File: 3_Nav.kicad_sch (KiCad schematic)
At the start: 38 parts, among them J401 GNSS, Q401 Q_NMOS, SW401 SW_Push, SW402 SW_Push, U403 STM32F446VETx, U404 W25Q128JVE, Y401 YXC YSX321SL

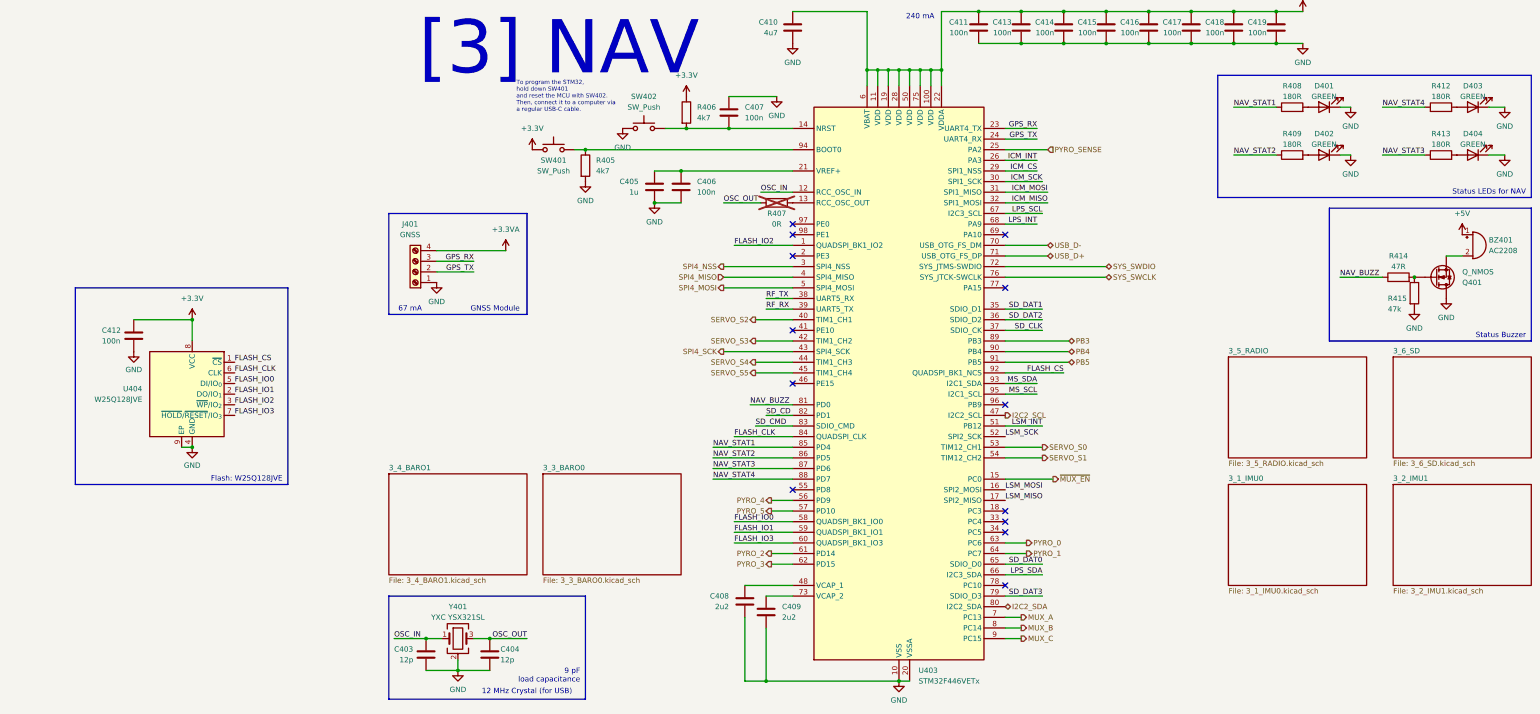
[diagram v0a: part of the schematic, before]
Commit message: Finished restructuring schematic
Most components that were on page 3 are now in their own page
Added high-frequency 4.7 uF capacitor to servo power line
Continuity sensing on pyrochannels is multiplexed to one ADC on NAV.
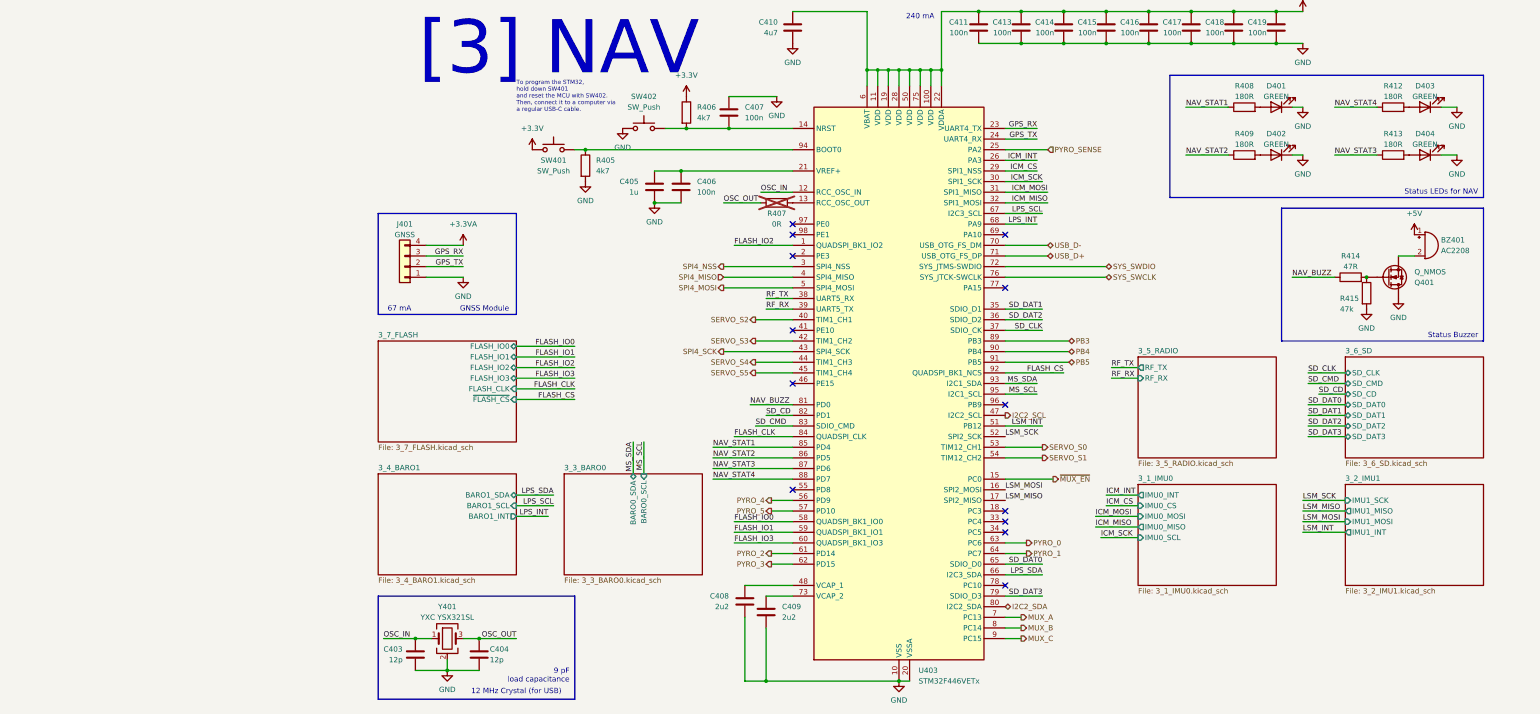
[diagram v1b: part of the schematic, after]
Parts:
- removed C412: 100n, Capacitor_SMD:C_0603_1608Metric, symbol Device:C
- removed J401: GNSS, TerminalBlock_MetzConnect:TerminalBlock_MetzConnect_Type055_RT01504HDWU_1x04_P5.00mm_Horizontal, symbol Connector:Screw_Terminal_01x04
- removed U404: W25Q128JVE, Package_SON:WSON-8-1EP_8x6mm_P1.27mm_EP3.4x4.3mm, symbol Memory_Flash:W25Q128JVE
- added J401: GNSS, Connector_JST:JST_XH_B4B-XH-A_1x04_P2.50mm_Vertical, symbol Connector_Generic:Conn_01x04
- C405, C406, C408, C409: footprint (none) -> Capacitor_SMD:C_0603_1608Metric
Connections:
- net +3.3VA: now also J401.4 (Pin_4)
- net GND: now also J401.1 (Pin_1)
- net GPS_RX: now also J401.3 (Pin_3)
- net GPS_TX: now also J401.2 (Pin_2)
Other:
- added sheet 3_7_FLASH (3_7_FLASH.kicad_sch)
- sheet 3_1_IMU0 ports: added IMU0_CS, IMU0_INT, IMU0_MISO, IMU0_MOSI, IMU0_SCL; removed none
- sheet 3_2_IMU1 ports: added IMU1_INT, IMU1_MISO, IMU1_MOSI, IMU1_SCK; removed none
- sheet 3_3_BARO0 ports: added BARO0_SCL, BARO0_SDA; removed none
- sheet 3_4_BARO1 ports: added BARO1_INT, BARO1_SCL, BARO1_SDA; removed none
- sheet 3_5_RADIO ports: added RF_RX, RF_TX; removed none
- sheet 3_6_SD ports: added SD_CD, SD_CLK, SD_CMD, SD_DAT0, SD_DAT1, SD_DAT2, SD_DAT3; removed none
- note removed: "Flash: W25Q128JVE"
- moved on the sheet: BZ401, C403, C404, D401, D402, D403, D404, Q401, R408, R409, R412, R413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

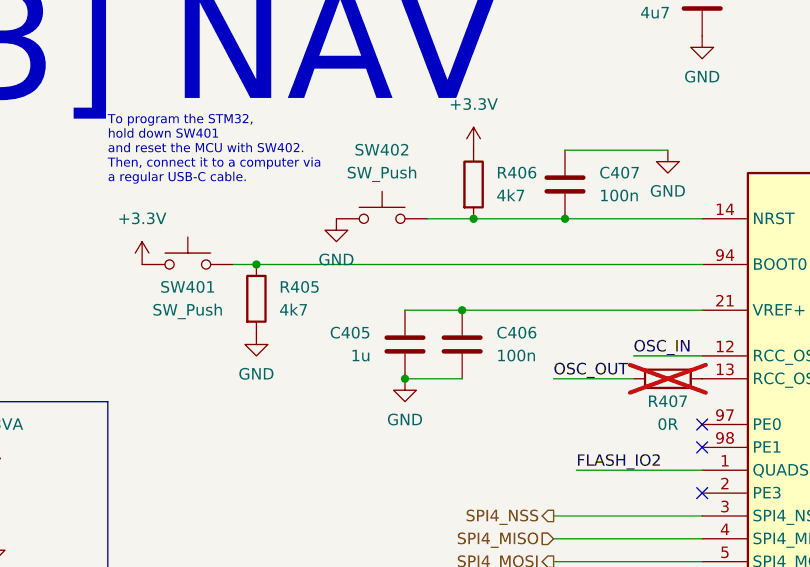
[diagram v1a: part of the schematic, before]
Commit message: Updated schematic so that servo GND and signal GND are no longer separate
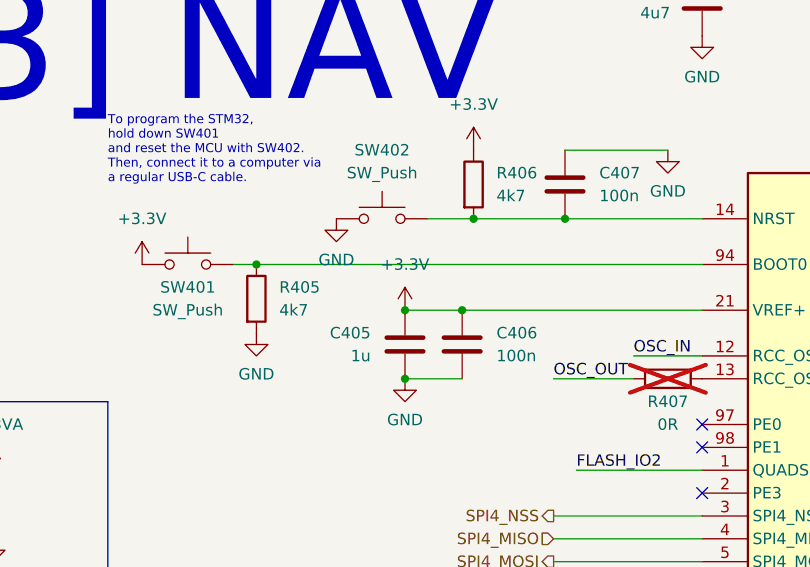
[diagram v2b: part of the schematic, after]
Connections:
- net +3.3V: now also C405.1, C406.1, U403.21 (VREF+)
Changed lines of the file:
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@@
 	)
 	(junction
+		(at 81.28 63.5)
+		(diameter 0)
+		(color 0 0 0 0)
+	)
+	(junction
 		(at 139.7 39.37)
 		(diameter 0)
@@
 					(unit 1)
 				)
+			)
+		)
+	)
+	(symbol
+		(lib_id "power:+3.3V")
+		(at 81.28 63.5 0)
+		(unit 1)
+		(body_style 1)
+		(exclude_from_sim no)
+		(in_bom yes)
+		(on_board yes)
+		(in_pos_files yes)
+		(dnp no)
+		(fields_autoplaced yes)
+		(property "Reference" "#PWR0403"
+			(at 81.28 67.31 0)
+			(hide yes)
+			(show_name no)
+			(do_not_autoplace no)
+			(effects
+				(font
+					(size 1.27 1.27)
+				)
+			)
+		)
+		(property "Value" "+3.3V"
+			(at 81.28 58.42 0)
+			(show_name no)
+			(do_not_autoplace no)
+			(effects
+				(font
+					(size 1.27 1.27)
+				)
+			)
+		)
+		(property "Footprint" ""
+			(at 81.28 63.5 0)
+			(hide yes)
+			(show_name no)
+			(do_not_autoplace no)
+			(effects
+				(font
+					(size 1.27 1.27)
+				)
+			)
+		)
+		(property "Datasheet" ""
+			(at 81.28 63.5 0)
+			(hide yes)
+			(show_name no)
+			(do_not_autoplace no)
+			(effects
+				(font
+					(size 1.27 1.27)
+				)
+			)
+		)
+		(property "Description" "Power symbol creates a global label with name \"+3.3V\""
+			(at 81.28 63.5 0)
+			(hide yes)
+			(show_name no)
+			(do_not_autoplace no)
+			(effects
+				(font
+					(size 1.27 1.27)
+				)
+			)
+		)
+		(pin "1"
+		)
+		(instances
+			(project "polaris"
+				(path "/cfb90e19-9fbe-47a1-a5ac-df522853d1d0/2c635aac-d26f-4bb6-b325-c281bd24fb50"
+					(reference "#PWR0403")
+					(unit 1)
+				)

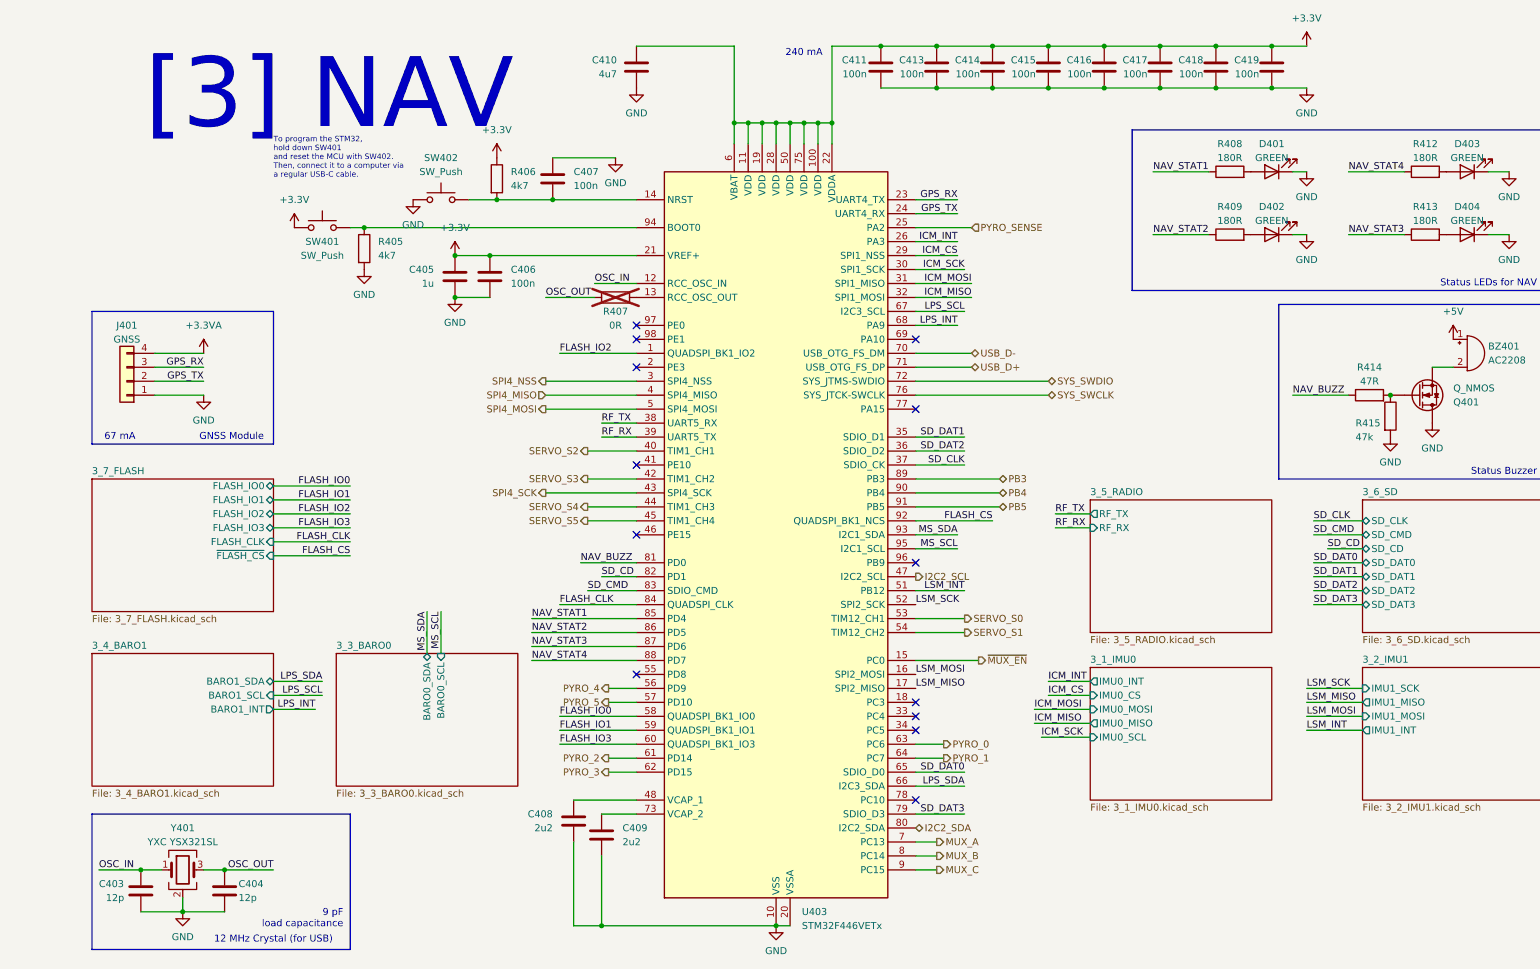
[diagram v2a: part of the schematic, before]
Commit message: Re-annotated schematic
Continued laying out traces on PCB
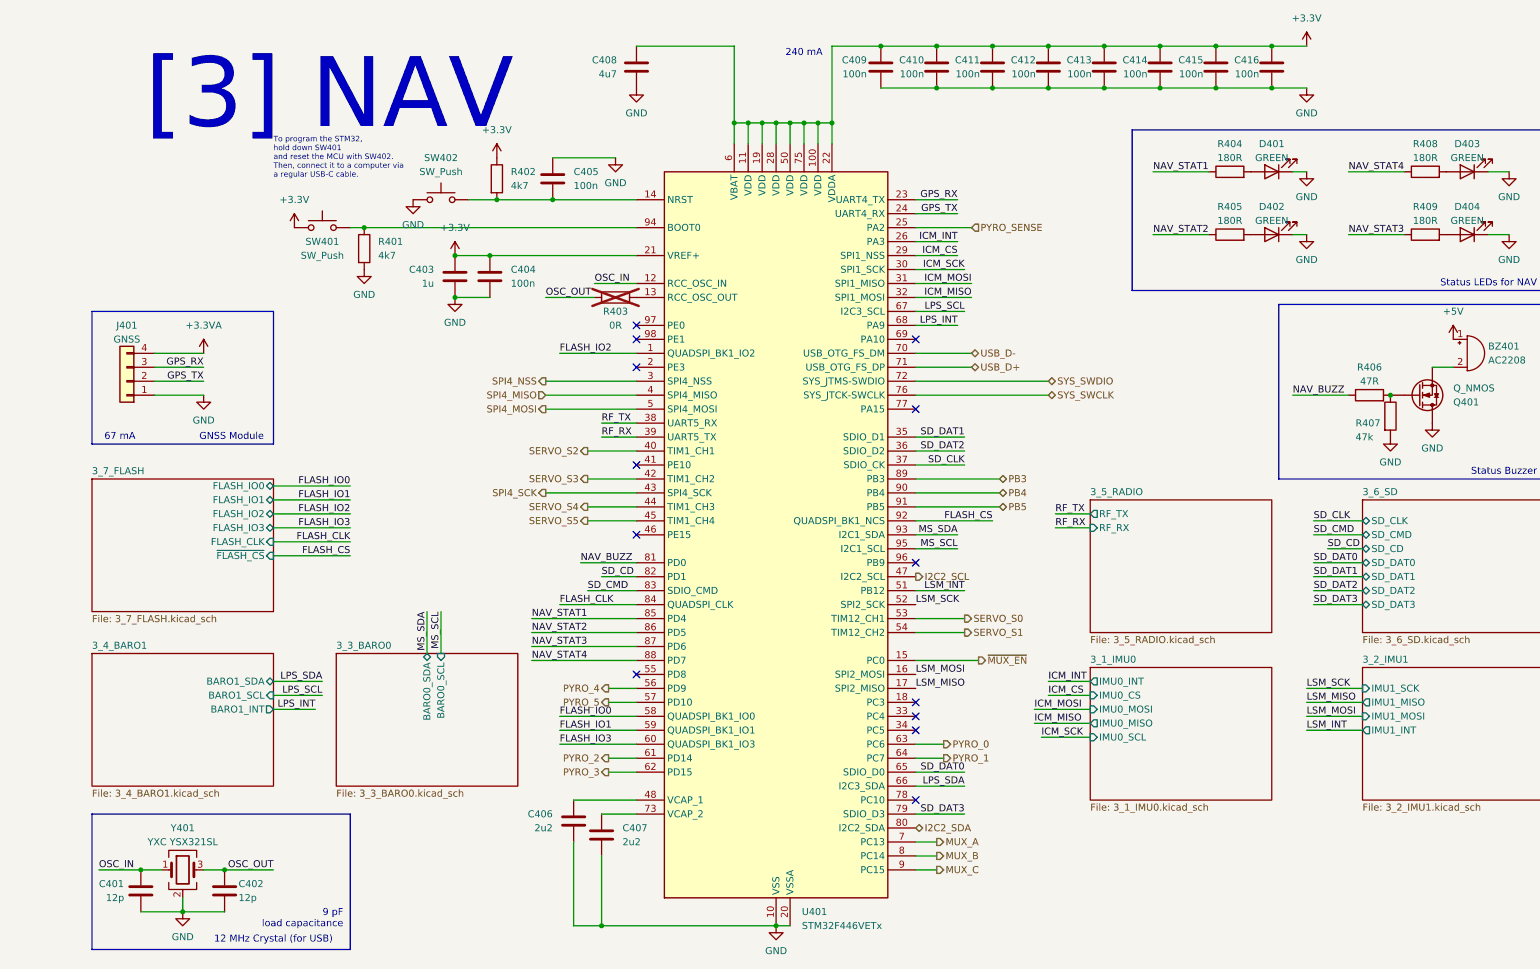
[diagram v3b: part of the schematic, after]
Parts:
- renumbered C403 to C401, C404 to C402, C405 to C403, C406 to C404, C407 to C405, C408 to C406, C409 to C407, C410 to C408, C411 to C409, C413 to C410, C414 to C411, C415 to C412, C416 to C413, C417 to C414, C418 to C415, C419 to C416, R405 to R401, R406 to R402, R407 to R403, R408 to R404, R409 to R405, R414 to R406, R415 to R407, R412 to R408, R413 to R409, U403 to U401
